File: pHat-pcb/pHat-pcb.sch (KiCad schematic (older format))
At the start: 12 parts, among them J1 Conn_02x20_Odd_Even, J2 Conn_01x24_Male, J3 Conn_Active_High, J4 Conn_Bat, J5 Conn_I2C, J8 Conn_Active_Low, SW1 SW_Push, U1 TPS61023_Breakout, U2 74HCT74, U3 DS3231M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

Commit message: Rev 1: layout complete
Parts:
- J8: footprint Connector_PinHeader_2.54mm:PinHeader_1x03_P2.54mm_Horizontal -> Connector_PinHeader_2.54mm:PinHeader_1x03_P2.54mm_Vertical
- R1: footprint Resistor_THT:R_Axial_DIN0207_L6.3mm_D2.5mm_P7.62mm_Horizontal -> Resistor_SMD:R_1206_3216Metric_Pad1.30x1.75mm_HandSolder
- U2, U4: footprint Package_DIP:DIP-14_W7.62mm_Socket -> user:SO-14_3.9x8.65mm_P1.27mm_HandSolder
- U3: footprint Package_SO:SOIC-16W_7.5x10.3mm_P1.27mm -> user:SOIC-16W_7.5x10.3mm_P1.27mm_HandSolder
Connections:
- wire segments 115 -> 122
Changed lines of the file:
@@
 Sheet 1 1
 Title "Pi Battery Management pHat"
-Date "2020-09-30"
+Date "2020-10-06"
 Rev "1"
 Comp "Bernhard Bablok"
@@
 F 0 "R1" V 7400 2750 50  0000 C CNN
 F 1 "10K" V 7300 2750 50  0000 C CNN
-F 2 "Resistor_THT:R_Axial_DIN0207_L6.3mm_D2.5mm_P7.62mm_Horizontal" V 7230 2750 50  0001 C CNN
+F 2 "Resistor_SMD:R_1206_3216Metric_Pad1.30x1.75mm_HandSolder" V 7230 2750 50  0001 C CNN
 F 3 "~" H 7300 2750 50  0001 C CNN
 	1    7300 2750
@@
 F 0 "U2" H 8450 3453 60  0000 C CNN
 F 1 "74HCT74" H 8450 3347 60  0000 C CNN
-F 2 "Package_DIP:DIP-14_W7.62mm_Socket" H 8700 2950 60  0001 L CNN
+F 2 "user:SO-14_3.9x8.65mm_P1.27mm_HandSolder" H 8700 2950 60  0001 L CNN
 F 3 "http://www.ti.com/general/docs/suppproductinfo.tsp?distId=10&gotoUrl=http%3A%2F%2Fwww.ti.com%2Flit%2Fgpn%2Fsn74hc74" H 8700 3050 60  0001 L CNN
 F 4 "296-1602-5-ND" H 8700 3150 60  0001 L CNN "Digi-Key_PN"
@@
 F 0 "J8" H 3350 4550 50  0000 R CNN
 F 1 "Conn_Active_Low" H 3600 4400 50  0000 R CNN
-F 2 "Connector_PinHeader_2.54mm:PinHeader_1x03_P2.54mm_Horizontal" H 3150 4150 50  0001 C CNN
+F 2 "Connector_PinHeader_2.54mm:PinHeader_1x03_P2.54mm_Vertical" H 3150 4150 50  0001 C CNN
 F 3 "~" H 3150 4150 50  0001 C CNN
 	1    3150 4150
@@
 Text Notes 750  5350 0    50   ~ 0
 on: High -> Low
-Text Label 3350 4150 0    50   ~ 0
+Text Label 3400 4050 0    50   ~ 0
 Vin
 $Comp
@@
 F 0 "U3" H 2100 4950 50  0000 C CNN
 F 1 "DS3231M" H 2100 4850 50  0000 C CNN
-F 2 "Package_SO:SOIC-16W_7.5x10.3mm_P1.27mm" H 2100 3750 50  0001 C CNN
+F 2 "user:SOIC-16W_7.5x10.3mm_P1.27mm_HandSolder" H 2100 3750 50  0001 C CNN
 F 3 "http://datasheets.maximintegrated.com/en/ds/DS3231.pdf" H 2370 4400 50  0001 C CNN
 	1    2100 4350
@@
 $EndComp
 Wire Wire Line
-	1100 4150 1600 4150
-Wire Wire Line
-	1100 4250 1600 4250
+	1100 4150 1300 4150
+Wire Wire Line
+	1100 4250 1400 4250
 $Comp
 L power:PWR_FLAG #FLG0101
@@
 L power:GND #PWR0105
 U 1 1 5F7A015C
-P 3350 4050
-F 0 "#PWR0105" H 3350 3800 50  0001 C CNN
-F 1 "GND" V 3355 3922 50  0000 R CNN
-F 2 "" H 3350 4050 50  0001 C CNN
-F 3 "" H 3350 4050 50  0001 C CNN
-	1    3350 4050
+P 3350 4150
+F 0 "#PWR0105" H 3350 3900 50  0001 C CNN
+F 1 "GND" V 3355 4022 50  0000 R CNN
+F 2 "" H 3350 4150 50  0001 C CNN
+F 3 "" H 3350 4150 50  0001 C CNN
+	1    3350 4150
 	0    -1   -1   0
 $EndComp
-Text Label 3350 4250 0    50   ~ 0
+Text Label 3400 4300 0    50   ~ 0
 1~PRE
 $Comp
@@
 1~PRE
 Wire Wire Line
-	6900 5250 7100 5250
-Wire Wire Line
 	6950 5400 7200 5400
 Wire Wire Line
 	7000 5700 7700 5700
-$Comp
-L power:PWR_FLAG #FLG0102
-U 1 1 5F799ED1
-P 7100 4850
-F 0 "#FLG0102" H 7100 4925 50  0001 C CNN
-F 1 "PWR_FLAG" V 7100 4977 50  0000 L CNN
-F 2 "" H 7100 4850 50  0001 C CNN
-F 3 "~" H 7100 4850 50  0001 C CNN
-	1    7100 4850
-	0    1    1    0
-$EndComp
-$Comp
-L power:PWR_FLAG #FLG0103
-U 1 1 5F79A6BB
-P 7200 5050
-F 0 "#FLG0103" H 7200 5125 50  0001 C CNN
-F 1 "PWR_FLAG" V 7200 5177 50  0000 L CNN
-F 2 "" H 7200 5050 50  0001 C CNN
-F 3 "~" H 7200 5050 50  0001 C CNN
-	1    7200 5050
-	0    1    1    0
-$EndComp
 Wire Wire Line
 	7200 5050 7200 5400
@@
 Wire Wire Line
 	7200 5400 7700 5400
-Wire Wire Line
-	7100 4850 7100 5250
-Connection ~ 7100 5250
-Wire Wire Line
-	7100 5250 7700 5250
 $Comp
 L User:74HC03 U4
@@
 F 0 "U4" H 2250 7370 50  0000 C CNN
 F 1 "74HC03" H 2250 7279 50  0000 C CNN
-F 2 "Package_DIP:DIP-14_W7.62mm_Socket" H 2250 6500 50  0001 L BNN
+F 2 "user:SO-14_3.9x8.65mm_P1.27mm_HandSolder" H 2250 6500 50  0001 L BNN
 F 3 "NXP" H 2250 6500 50  0001 L BNN
 F 4 "1085231" H 2250 6500 50  0001 L BNN "Feld4"
@@
 Text Notes 3200 6000 0    50   ~ 0
 on: High -> Low
+Text Label 7450 5200 0    50   ~ 0
+Vin
+Wire Wire Line
+	7450 5200 7450 5250
+Connection ~ 7450 5250
+Wire Wire Line
+	7450 5250 7700 5250
+Wire Wire Line
+	6900 5250 7450 5250
+Text Label 1400 3750 0    50   ~ 0
+GPIO2(SDA1)
+Text Label 1300 3600 0    50   ~ 0
+GPIO3(SCL1)
+Wire Wire Line
+	1300 3600 1300 4150
+Connection ~ 1300 4150
+Wire Wire Line
+	1300 4150 1600 4150
+Wire Wire Line
+	1400 3750 1400 4250
+Connection ~ 1400 4250
+Wire Wire Line
+	1400 4250 1600 4250
+$Comp
+L power:GND #PWR0109
+U 1 1 5F805DAA
+P 7200 5050
+F 0 "#PWR0109" H 7200 4800 50  0001 C CNN
+F 1 "GND" V 7205 4922 50  0000 R CNN
+F 2 "" H 7200 5050 50  0001 C CNN
+F 3 "" H 7200 5050 50  0001 C CNN
+	1    7200 5050
+	0    -1   -1   0
+$EndComp
+Wire Wire Line
+	3350 4250 3350 4300
+Wire Wire Line
+	3350 4300 3400 4300
+Wire Wire Line
+	3350 4050 3400 4050
 $EndSCHEMATC

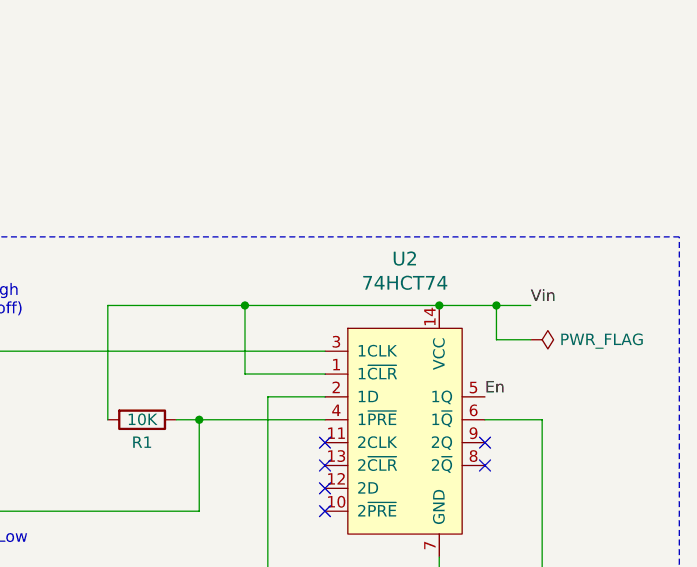
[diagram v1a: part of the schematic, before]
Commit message: bugfix: replace 74HCT74 with 74HC74
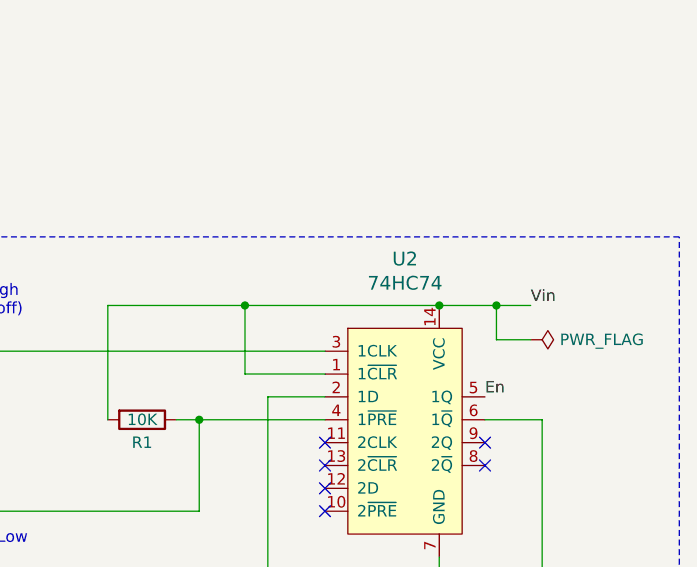
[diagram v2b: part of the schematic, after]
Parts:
- U2: value 74HCT74 -> 74HC74
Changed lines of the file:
@@
 Sheet 1 1
 Title "Pi Battery Management pHat"
-Date "2020-10-06"
+Date "2020-10-12"
 Rev "1"
 Comp "Bernhard Bablok"
@@
 P 8500 2750
 F 0 "U2" H 8450 3453 60  0000 C CNN
-F 1 "74HCT74" H 8450 3347 60  0000 C CNN
+F 1 "74HC74" H 8450 3347 60  0000 C CNN
 F 2 "user:SO-14_3.9x8.65mm_P1.27mm_HandSolder" H 8700 2950 60  0001 L CNN
 F 3 "http://www.ti.com/general/docs/suppproductinfo.tsp?distId=10&gotoUrl=http%3A%2F%2Fwww.ti.com%2Flit%2Fgpn%2Fsn74hc74" H 8700 3050 60  0001 L CNN

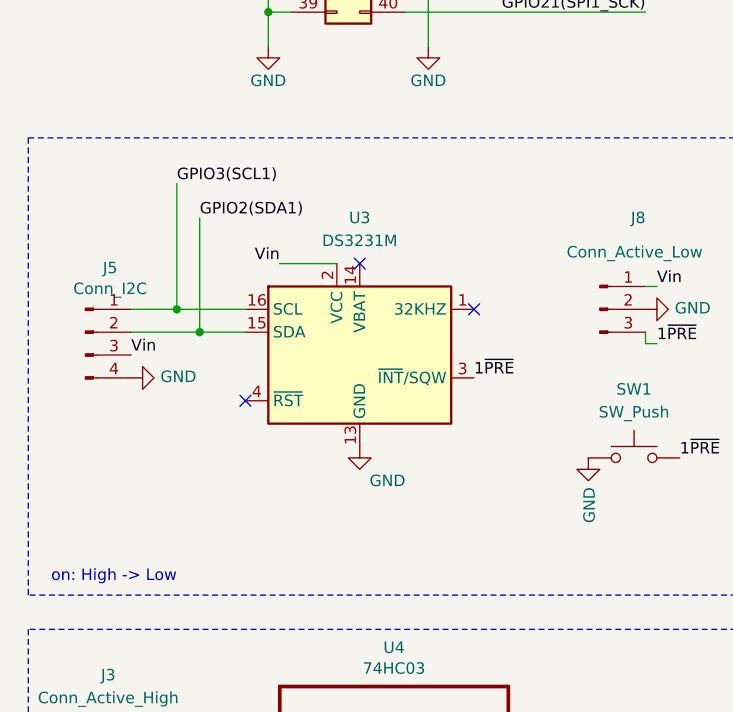
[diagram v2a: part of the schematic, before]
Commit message: added capacitor to DS3231
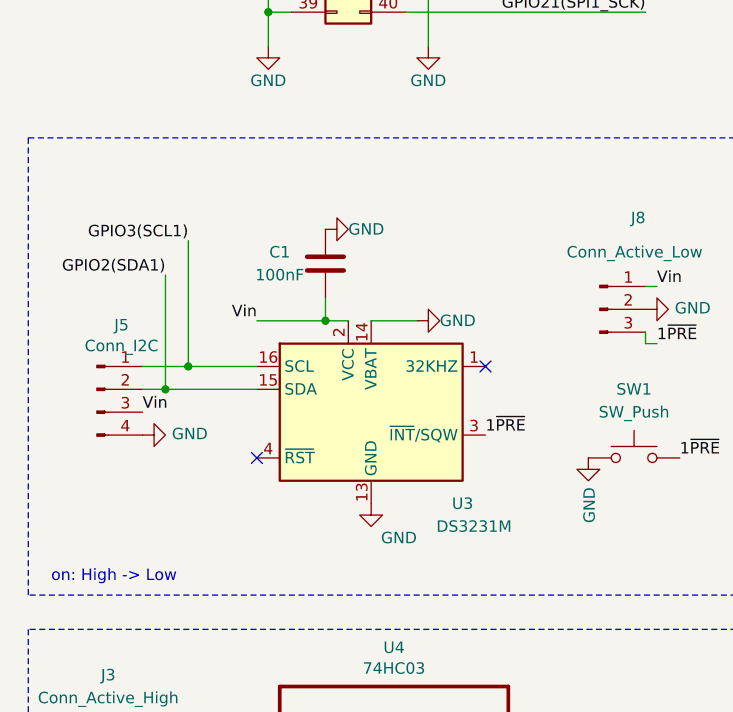
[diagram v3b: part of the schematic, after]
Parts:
- added C1: 100nF, Capacitor_SMD:C_1206_3216Metric_Pad1.33x1.80mm_HandSolder, symbol Device:C
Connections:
- wire segments 122 -> 125
- no-connect marks 20 -> 19
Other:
- moved on the sheet: J5, U3
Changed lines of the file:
@@
 Sheet 1 1
 Title "Pi Battery Management pHat"
-Date "2020-10-12"
-Rev "1"
+Date "2020-10-17"
+Rev "2"
 Comp "Bernhard Bablok"
 Comment1 "https://github.com/bablokb/pcb-pi-batman"
@@
 L Timer_RTC:DS3231M U3
 U 1 1 5F75DC2A
-P 2100 4350
-F 0 "U3" H 2100 4950 50  0000 C CNN
-F 1 "DS3231M" H 2100 4850 50  0000 C CNN
-F 2 "user:SOIC-16W_7.5x10.3mm_P1.27mm_HandSolder" H 2100 3750 50  0001 C CNN
-F 3 "http://datasheets.maximintegrated.com/en/ds/DS3231.pdf" H 2370 4400 50  0001 C CNN
-	1    2100 4350
+P 2150 4600
+F 0 "U3" H 2550 4200 50  0000 C CNN
+F 1 "DS3231M" H 2600 4100 50  0000 C CNN
+F 2 "user:SOIC-16W_7.5x10.3mm_P1.27mm_HandSolder" H 2150 4000 50  0001 C CNN
+F 3 "http://datasheets.maximintegrated.com/en/ds/DS3231.pdf" H 2420 4650 50  0001 C CNN
+	1    2150 4600
 	1    0    0    -1
 $EndComp
@@
 L Connector:Conn_01x04_Male J5
 U 1 1 5F760C28
-P 900 4250
-F 0 "J5" H 1008 4531 50  0000 C CNN
-F 1 "Conn_I2C" H 1008 4440 50  0000 C CNN
-F 2 "Connector_PinHeader_2.54mm:PinHeader_1x04_P2.54mm_Vertical" H 900 4250 50  0001 C CNN
-F 3 "~" H 900 4250 50  0001 C CNN
-	1    900  4250
+P 950 4500
+F 0 "J5" H 1058 4781 50  0000 C CNN
+F 1 "Conn_I2C" H 1058 4690 50  0000 C CNN
+F 2 "Connector_PinHeader_2.54mm:PinHeader_1x04_P2.54mm_Vertical" H 950 4500 50  0001 C CNN
+F 3 "~" H 950 4500 50  0001 C CNN
+	1    950  4500
 	1    0    0    -1
 $EndComp
@@
 Text Label 6650 5850 0    50   ~ 0
 GPIO16
-NoConn ~ 2600 4150
+NoConn ~ 2650 4400
 $Comp
 L power:GND #PWR02
 U 1 1 5F783D0C
-P 2100 4750
-F 0 "#PWR02" H 2100 4500 50  0001 C CNN
-F 1 "GND" H 2300 4600 50  0000 R CNN
-F 2 "" H 2100 4750 50  0001 C CNN
-F 3 "" H 2100 4750 50  0001 C CNN
-	1    2100 4750
-	1    0    0    -1
-$EndComp
-NoConn ~ 1600 4550
-NoConn ~ 2100 3950
-Text Label 1750 3950 2    50   ~ 0
+P 2150 5000
+F 0 "#PWR02" H 2150 4750 50  0001 C CNN
+F 1 "GND" H 2350 4850 50  0000 R CNN
+F 2 "" H 2150 5000 50  0001 C CNN
+F 3 "" H 2150 5000 50  0001 C CNN
+	1    2150 5000
+	1    0    0    -1
+$EndComp
+NoConn ~ 1650 4800
+Text Label 1650 4200 2    50   ~ 0
 Vin
-Wire Wire Line
-	1750 3950 2000 3950
-Text Label 1100 4350 0    50   ~ 0
+Text Label 1150 4600 0    50   ~ 0
 Vin
 $Comp
 L power:GND #PWR01
 U 1 1 5F7903D4
-P 1100 4450
-F 0 "#PWR01" H 1100 4200 50  0001 C CNN
-F 1 "GND" V 1105 4322 50  0000 R CNN
-F 2 "" H 1100 4450 50  0001 C CNN
-F 3 "" H 1100 4450 50  0001 C CNN
-	1    1100 4450
+P 1150 4700
+F 0 "#PWR01" H 1150 4450 50  0001 C CNN
+F 1 "GND" V 1155 4572 50  0000 R CNN
+F 2 "" H 1150 4700 50  0001 C CNN
+F 3 "" H 1150 4700 50  0001 C CNN
+	1    1150 4700
 	0    -1   -1   0
 $EndComp
 Wire Wire Line
-	1100 4150 1300 4150
-Wire Wire Line
-	1100 4250 1400 4250
+	1150 4400 1350 4400
+Wire Wire Line
+	1150 4500 1250 4500
 $Comp
 L power:PWR_FLAG #FLG0101
@@
 Wire Wire Line
 	7550 2750 8100 2750
-Text Label 2600 4450 0    50   ~ 0
+Text Label 2650 4700 0    50   ~ 0
 1~PRE
 Wire Wire Line
@@
 Wire Wire Line
 	6900 5250 7450 5250
-Text Label 1400 3750 0    50   ~ 0
+Text Label 1250 4000 2    50   ~ 0
 GPIO2(SDA1)
-Text Label 1300 3600 0    50   ~ 0
+Text Label 1350 3850 2    50   ~ 0
 GPIO3(SCL1)
 Wire Wire Line
-	1300 3600 1300 4150
-Connection ~ 1300 4150
-Wire Wire Line
-	1300 4150 1600 4150
-Wire Wire Line
-	1400 3750 1400 4250
-Connection ~ 1400 4250
-Wire Wire Line
-	1400 4250 1600 4250
+	1350 3850 1350 4400
+Connection ~ 1350 4400
+Wire Wire Line
+	1350 4400 1650 4400
+Wire Wire Line
+	1250 4000 1250 4500
+Connection ~ 1250 4500
+Wire Wire Line
+	1250 4500 1650 4500
 $Comp
 L power:GND #PWR0109
@@
 Wire Wire Line
 	3350 4050 3400 4050
+$Comp
+L power:GND #PWR0110
+U 1 1 5F8B2D56
+P 2350 4200
+F 0 "#PWR0110" H 2350 3950 50  0001 C CNN
+F 1 "GND" V 2350 4100 50  0000 R CNN
+F 2 "" H 2350 4200 50  0001 C CNN
+F 3 "" H 2350 4200 50  0001 C CNN
+	1    2350 4200
+	0    -1   -1   0
+$EndComp
+$Comp
+L Device:C C1
+U 1 1 5F8B3C5A
+P 1950 3950
+F 0 "C1" H 1750 4000 50  0000 C CNN
+F 1 "100nF" H 1750 3900 50  0000 C CNN
+F 2 "Capacitor_SMD:C_1206_3216Metric_Pad1.33x1.80mm_HandSolder" H 1988 3800 50  0001 C CNN
+F 3 "~" H 1950 3950 50  0001 C CNN
+	1    1950 3950
+	1    0    0    -1
+$EndComp
+Wire Wire Line
+	2150 4200 2350 4200
+$Comp
+L power:GND #PWR0111
+U 1 1 5F8F23AD
+P 1950 3800
+F 0 "#PWR0111" H 1950 3550 50  0001 C CNN
+F 1 "GND" V 1950 3700 50  0000 R CNN
+F 2 "" H 1950 3800 50  0001 C CNN
+F 3 "" H 1950 3800 50  0001 C CNN
+	1    1950 3800
+	0    -1   -1   0
+$EndComp
+Wire Wire Line
+	1650 4200 1950 4200
+Wire Wire Line
+	1950 4100 1950 4200
+Connection ~ 1950 4200
+Wire Wire Line
+	1950 4200 2050 4200
 $EndSCHEMATC

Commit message: removed external LBO connector
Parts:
- J4: footprint TerminalBlock_TE-Connectivity:TerminalBlock_TE_282834-4_1x04_P2.54mm_Horizontal -> TerminalBlock_TE-Connectivity:TerminalBlock_TE_282834-3_1x03_P2.54mm_Horizontal; symbol Connector:Conn_01x04_Female -> Connector:Conn_01x03_Female
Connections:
- net labels removed: LBO
- wire segments 125 -> 124
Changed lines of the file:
@@
 $EndComp
 $Comp
-L Connector:Conn_01x04_Female J4
+L Connector:Conn_01x03_Female J4
 U 1 1 5F762AD7
-P 6450 5550
-F 0 "J4" H 6342 5125 50  0000 C CNN
-F 1 "Conn_Bat" H 6342 5216 50  0000 C CNN
-F 2 "TerminalBlock_TE-Connectivity:TerminalBlock_TE_282834-4_1x04_P2.54mm_Horizontal" H 6450 5550 50  0001 C CNN
-F 3 "~" H 6450 5550 50  0001 C CNN
-	1    6450 5550
+P 6450 5450
+F 0 "J4" H 6342 5025 50  0000 C CNN
+F 1 "Conn_Bat" H 6342 5116 50  0000 C CNN
+F 2 "TerminalBlock_TE-Connectivity:TerminalBlock_TE_282834-3_1x03_P2.54mm_Horizontal" H 6450 5450 50  0001 C CNN
+F 3 "~" H 6450 5450 50  0001 C CNN
+	1    6450 5450
 	-1   0    0    1
 $EndComp
@@
 Text Label 6500 2450 2    50   ~ 0
 GPIO26
-Text Label 6650 5850 0    50   ~ 0
-GPIO16
 NoConn ~ 2650 4400
 $Comp
@@
 	6900 5700 7000 5700
 Connection ~ 7000 5700
-Text Label 6650 5650 0    50   ~ 0
-LBO
 Wire Wire Line
 	9000 2400 8850 2400
@@
 (74HC05 not available, so use NAND as inverter:\nnot x = x nand x)
 Wire Wire Line
-	6650 5850 6650 5650
-Wire Wire Line
 	6450 3150 7550 3150
